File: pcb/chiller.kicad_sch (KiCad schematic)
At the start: 67 parts, among them J1 Temp sensor 1, J10 Fan, J11 Display, J12 Debug, J13 Conn_01x04, J14 Flow sensor, J15 Buzzer, J2 Temp sensor 2, J3 Ext, J4 Mains in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

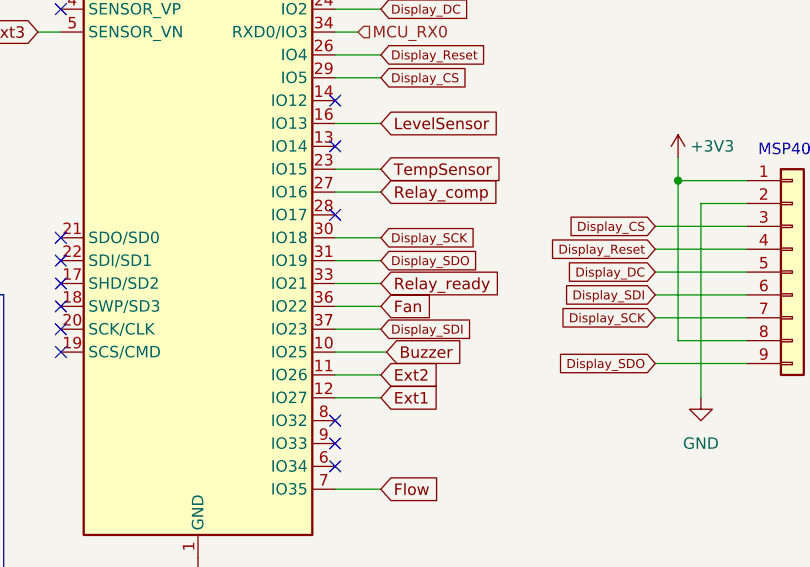
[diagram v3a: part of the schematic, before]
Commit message: Finish routing.
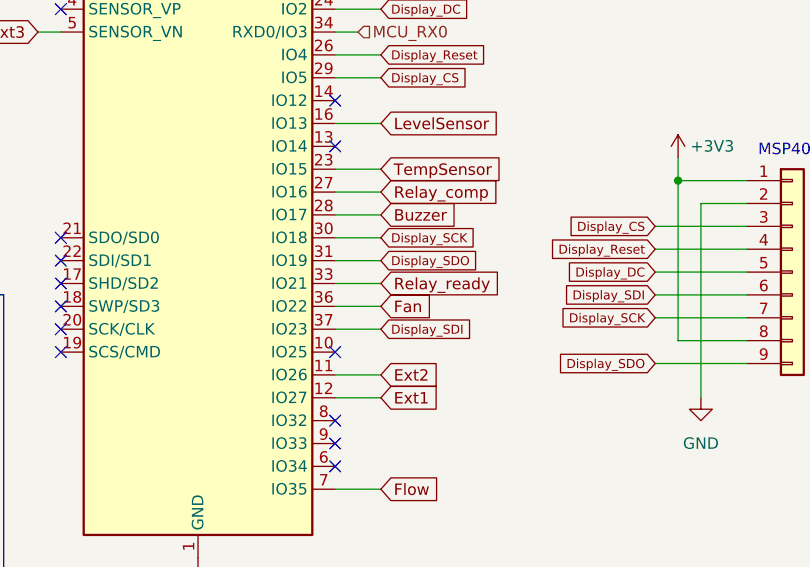
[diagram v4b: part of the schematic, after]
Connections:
- net Buzzer: now also U1.28 (IO17); no longer U1.10 (IO25)
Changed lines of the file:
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@@
   (no_connect (at 58.42 34.29))
   (no_connect (at 138.43 132.08))
+  (no_connect (at 88.9 72.39))
   (no_connect (at 88.9 82.55))
   (no_connect (at 88.9 49.53))
   (no_connect (at 88.9 85.09))
-  (no_connect (at 88.9 57.15))
   (no_connect (at 88.9 80.01))
   (no_connect (at 255.27 41.91))
@@
     (stroke (width 0) (type default))
   )
+  (wire (pts (xy 88.9 57.15) (xy 93.98 57.15))
+    (stroke (width 0) (type default))
+  )
   (wire (pts (xy 63.5 139.7) (xy 63.5 121.92))
     (stroke (width 0) (type default))
@@
   )
   (wire (pts (xy 63.5 142.24) (xy 63.5 139.7))
-    (stroke (width 0) (type default))
-  )
-  (wire (pts (xy 88.9 72.39) (xy 94.615 72.39))
     (stroke (width 0) (type default))
   )
@@
     )
   )
-  (global_label "Buzzer" (shape input) (at 94.615 72.39 0) (fields_autoplaced)
-    (effects (font (size 1.27 1.27)) (justify left))
-    (property "Intersheetrefs" "${INTERSHEET_REFS}" (at 103.9502 72.39 0)
-      (effects (font (size 1.27 1.27)) (justify left) hide)
-    )
+  (global_label "Buzzer" (shape input) (at 93.98 57.15 0) (fields_autoplaced)
+    (effects (font (size 1.27 1.27)) (justify left))
+    (property "Intersheetrefs" "${INTERSHEET_REFS}" (at 103.3152 57.15 0)
+      (effects (font (size 1.27 1.27)) (justify left) hide)
+    )

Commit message: Fix footprint.
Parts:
- D8: footprint Diode_SMD:D_SMC -> Diode_SMD:D_SMA
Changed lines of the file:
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@@
       (effects (font (size 1.27 1.27)) (justify left))
     )
-    (property "Footprint" "Diode_SMD:D_SMC" (at 248.92 144.78 0)
+    (property "Footprint" "Diode_SMD:D_SMA" (at 248.92 144.78 0)
       (effects (font (size 1.27 1.27)) hide)
     )

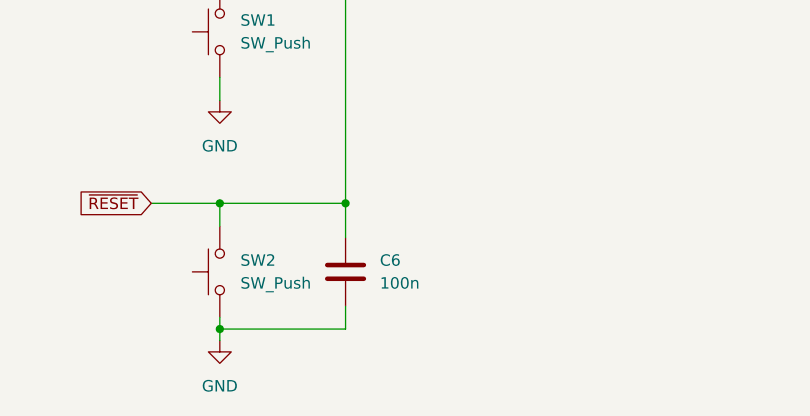
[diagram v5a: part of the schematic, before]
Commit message: Allow a few temp sensor errors before panicking.
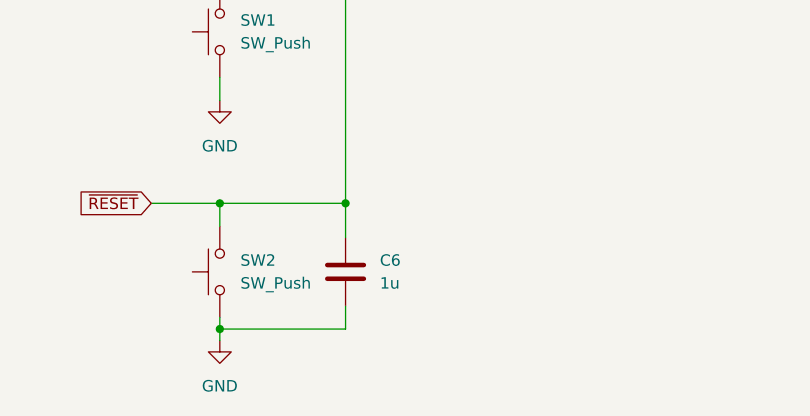
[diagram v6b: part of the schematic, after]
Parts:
- C6: value 100n -> 1u
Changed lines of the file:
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@@
       (effects (font (size 1.27 1.27)) (justify left))
     )
-    (property "Value" "100n" (at 259.08 246.3799 0)
+    (property "Value" "1u" (at 259.08 246.3799 0)
       (effects (font (size 1.27 1.27)) (justify left))
     )

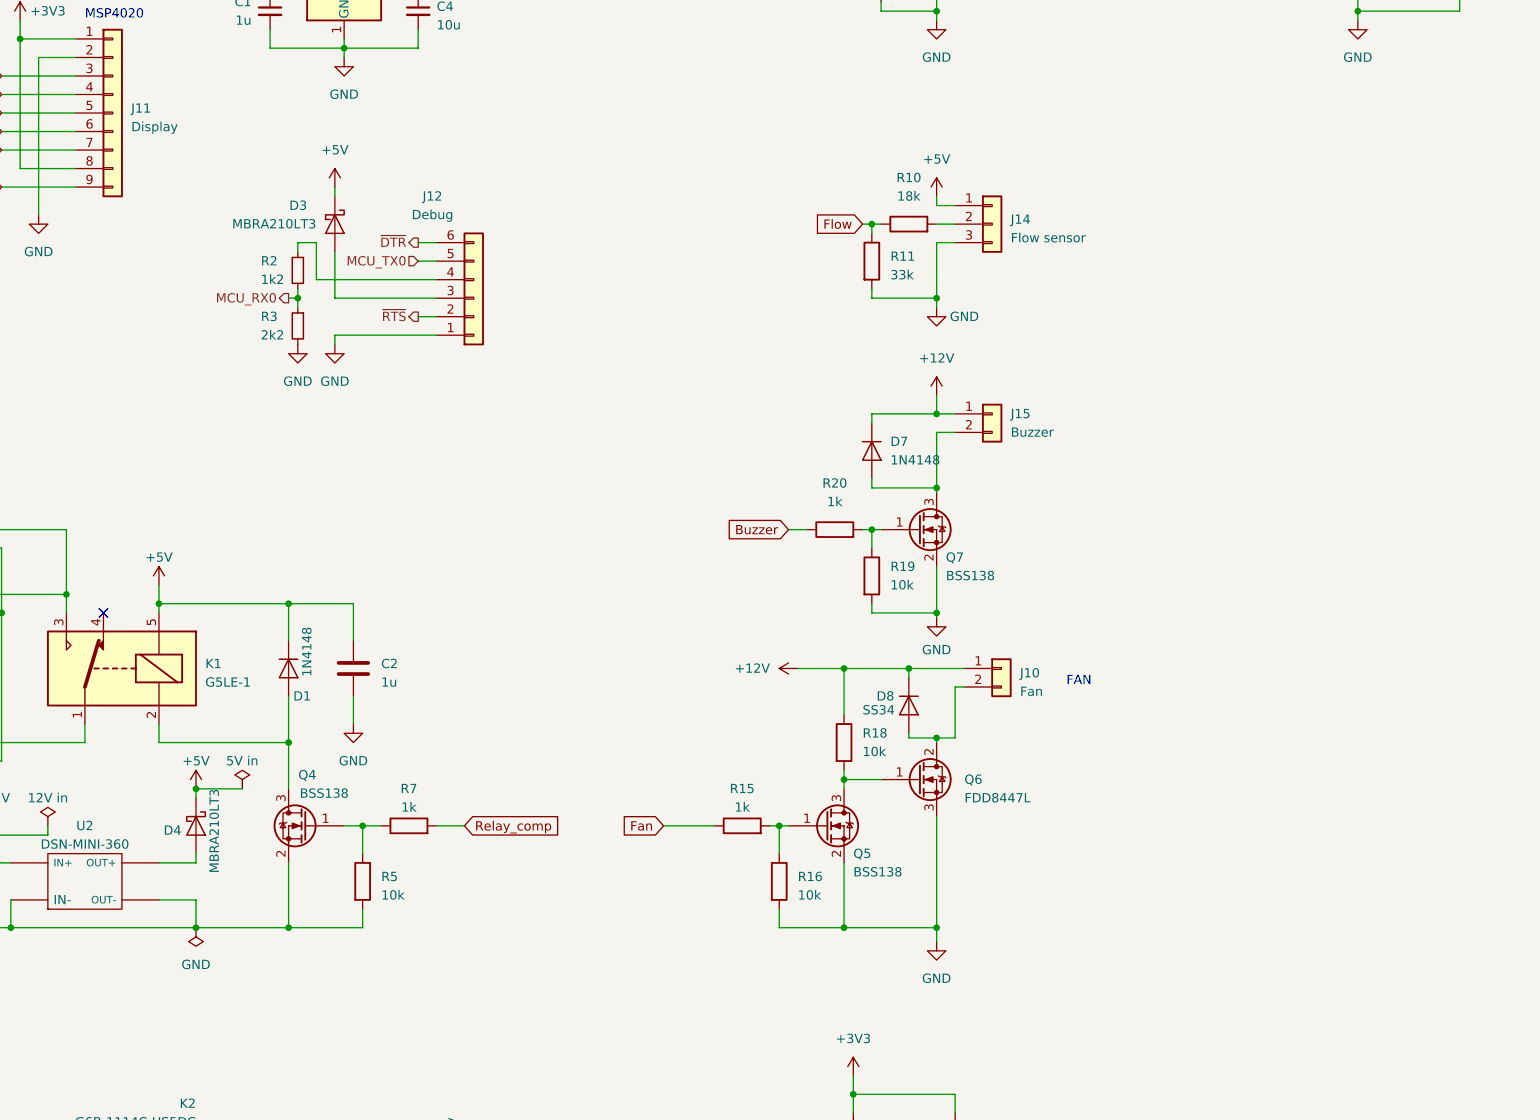
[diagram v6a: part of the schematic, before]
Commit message: Add inverters, stitching vias.
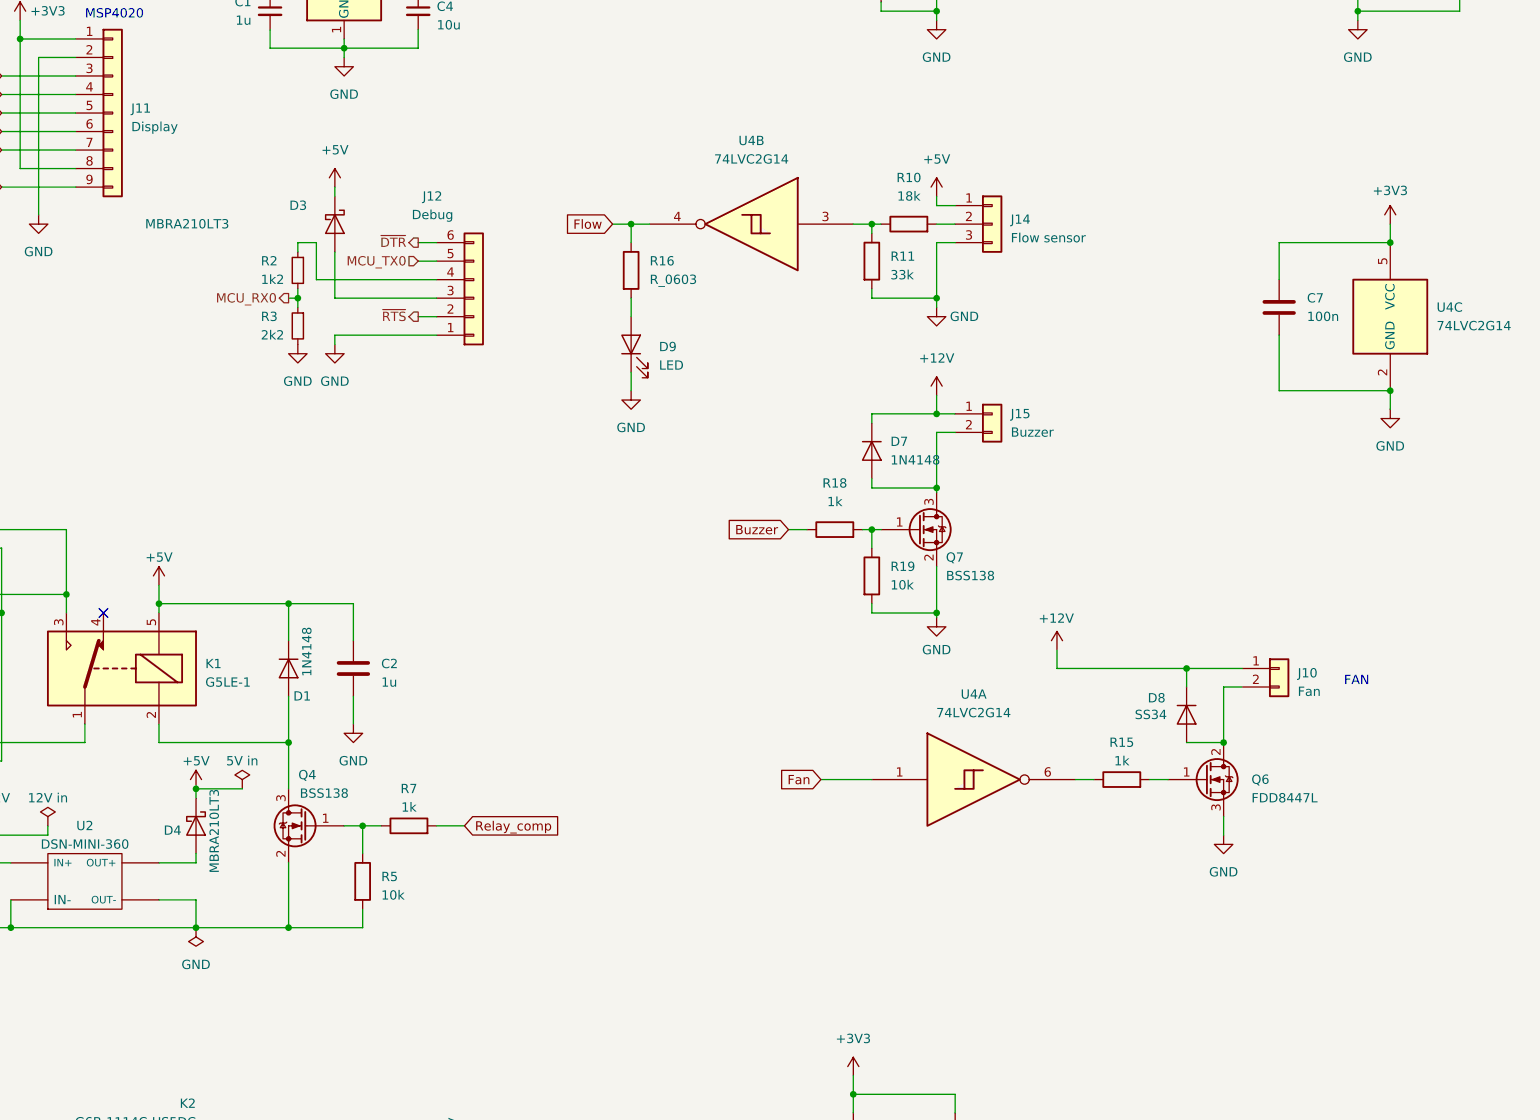
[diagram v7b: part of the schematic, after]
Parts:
- removed Q5: BSS138, Package_TO_SOT_SMD:SOT-23, symbol Device:Q_NMOS_GSD
- removed R16, R18: 10k, Resistor_SMD:R_0603_1608Metric, symbol Device:R
- added C7: 100n, Capacitor_SMD_AKL:C_0603_1608Metric, symbol Capacitor_AKL:C_0603
- added D9: LED, LED_SMD:LED_0201_0603Metric, symbol Device:LED
- added R16: R_0603, Resistor_SMD_AKL:R_0603_1608Metric, symbol Resistor_AKL:R_0603
- added U4: 74LVC2G14, Package_TO_SOT_SMD:SOT-23-6, symbol 74xGxx:74LVC2G14
- D8: footprint Diode_SMD:D_SMA -> (none)
- renumbered R20 to R18
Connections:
- net +3V3: now also C7.1, U4.5 (VCC)
- net Fan: now also U4.1; no longer R15.1
- net Flow: now also R16.1, U4.4; no longer R10.1, R11.1
- net GND: now also C7.2, D9.1 (K), U4.2 (GND)
- net at R15.2: now also Q6.1 (G)
- new net: R10.1, R11.1, U4.3
- new net: D9.2 (A), R16.2
- new net: R15.1, U4.6
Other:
- moved on the sheet: J10, Q6, R15

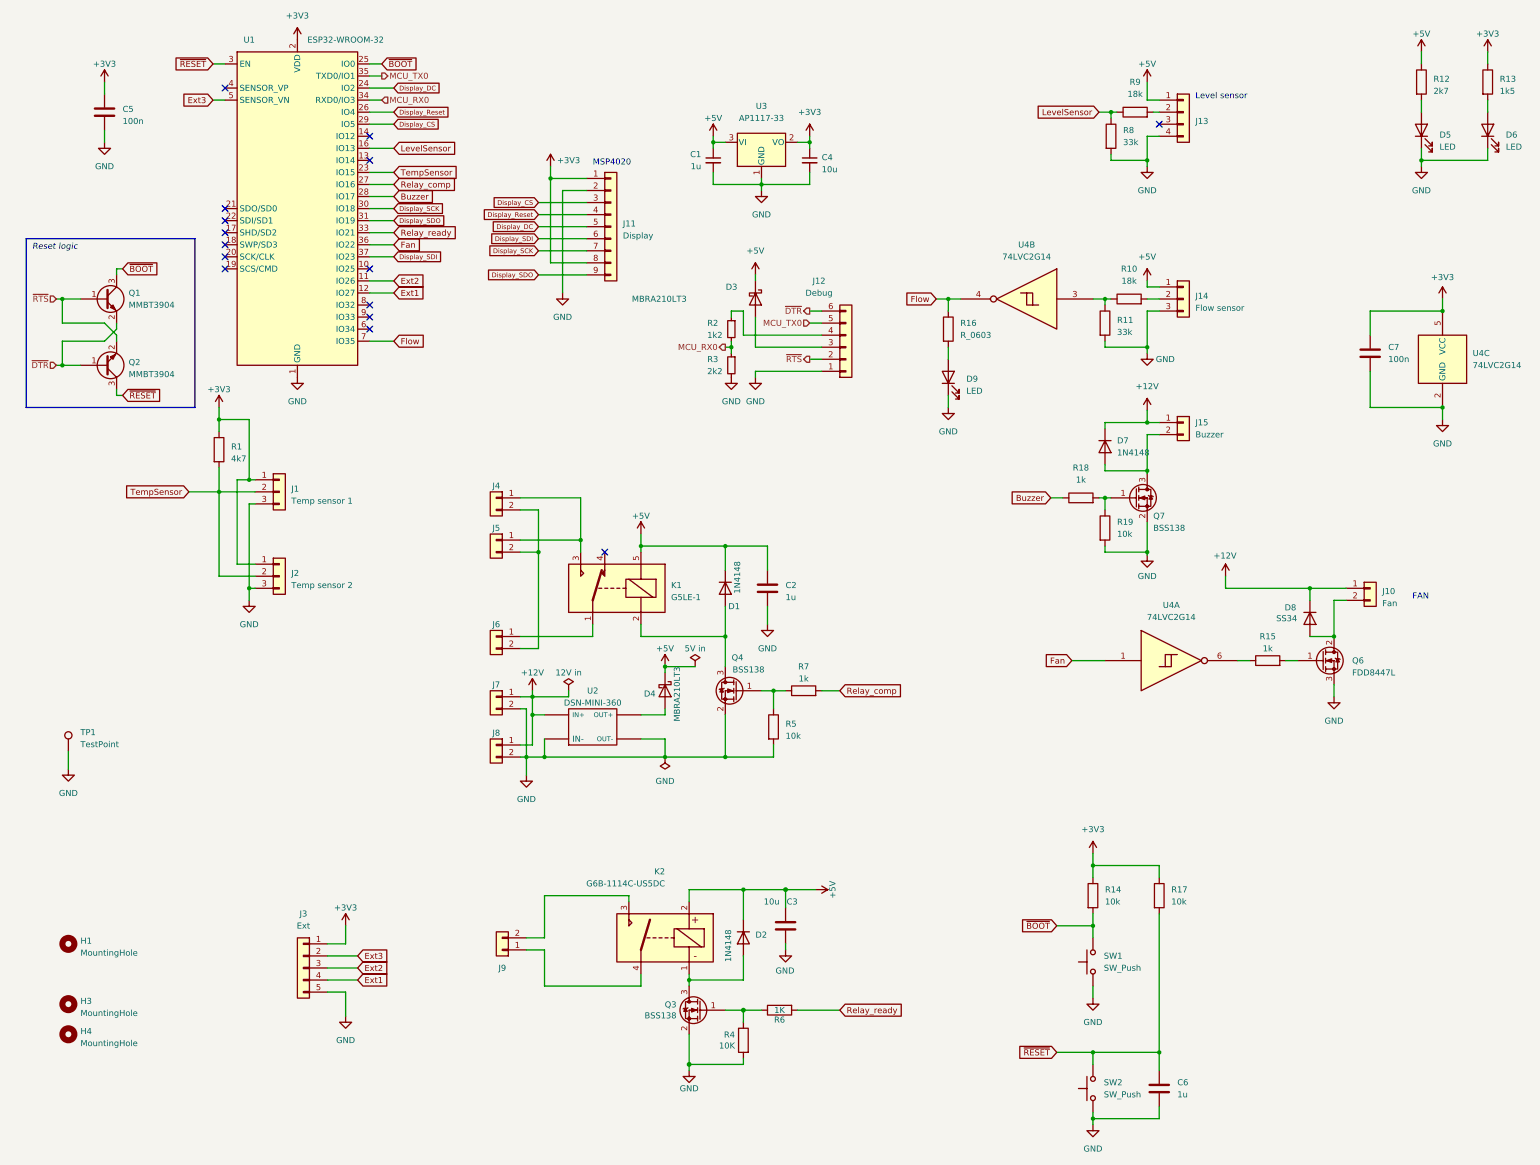
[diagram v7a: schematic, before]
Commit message: Fix ERC issues.
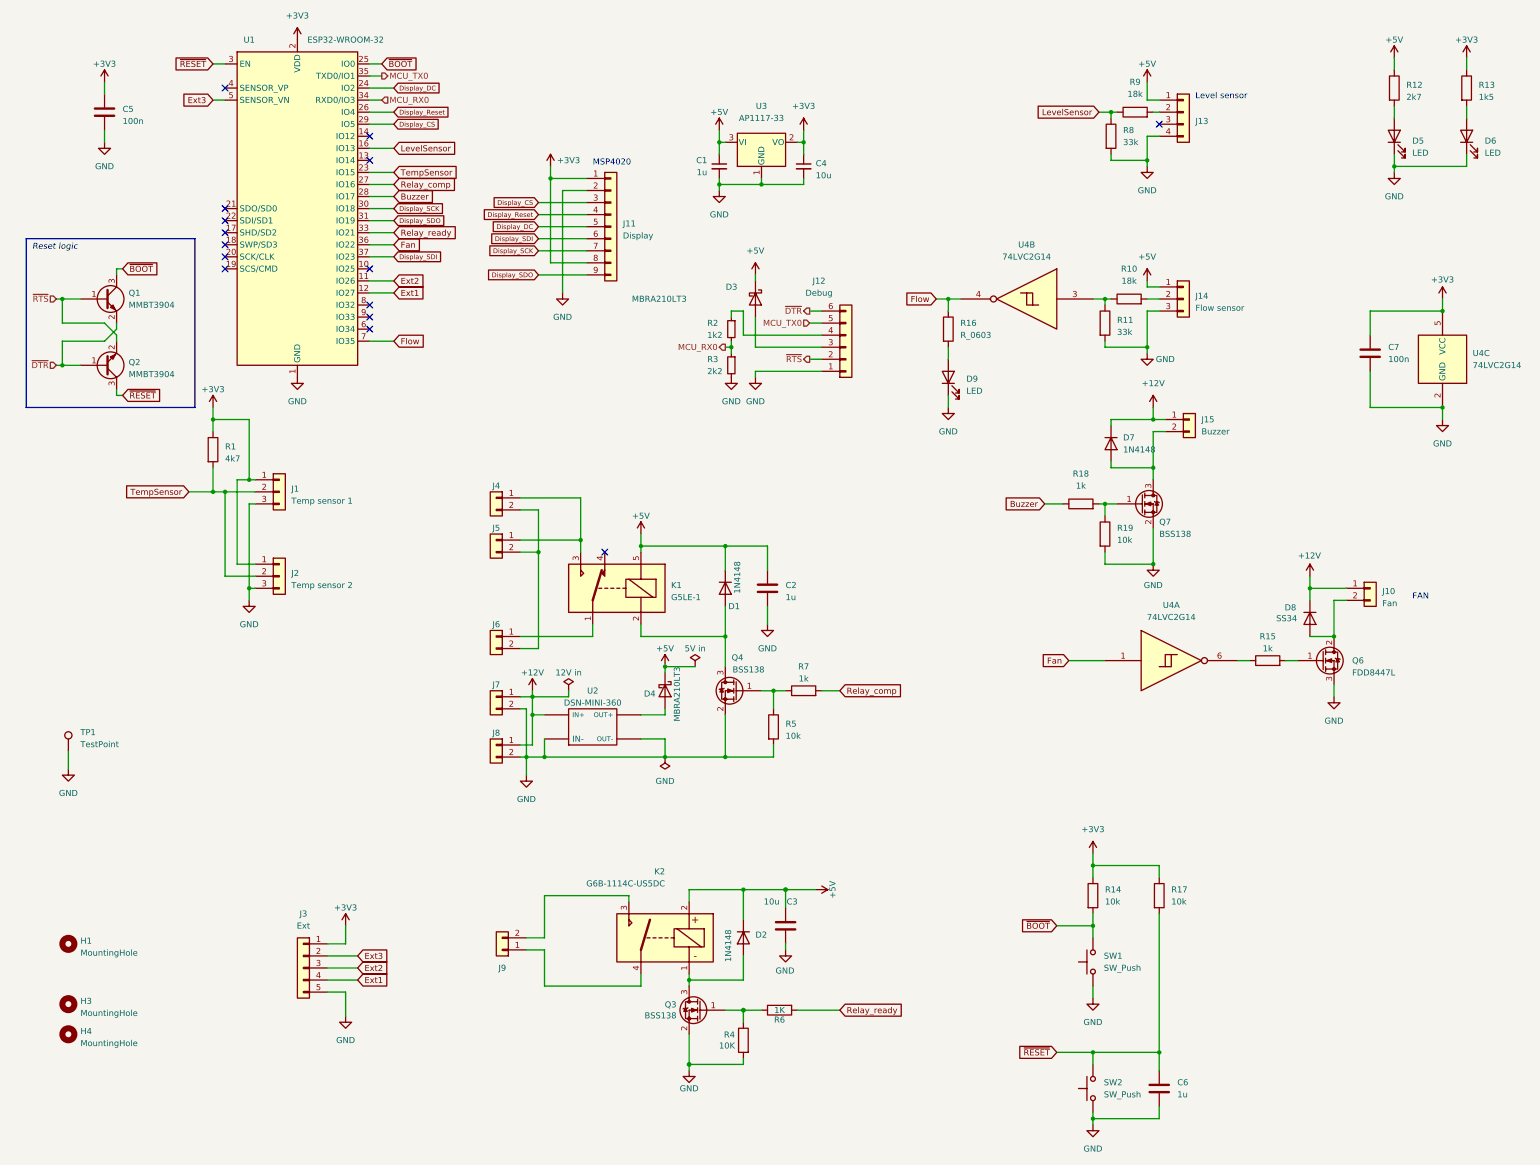
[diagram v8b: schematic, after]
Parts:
- C1, C2, C3, C4, C5, C6: footprint Capacitor_SMD:C_0603_1608Metric -> Capacitor_SMD_AKL:C_0603_1608Metric
- D8: footprint (none) -> Diode_SMD:D_SMA
- R1, R10, R11, R12, R13, R14, R15, R17, R18, R19, R2, R3, R4, R5, R6, R7, R8, R9: footprint Resistor_SMD:R_0603_1608Metric -> Resistor_SMD_AKL:R_0603_1608Metric
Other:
- moved on the sheet: C1, C4, D5, D6, D7, J15, Q7, R1, R12, R13, R18, R19
